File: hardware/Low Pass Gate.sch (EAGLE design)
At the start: 99 parts, among them IC1 TL072, IC2 LM397, IC3 TL072, IC4 TL072, IC5 LM397, IC6 TL072, P1 POWER_SIMPLE10_SHROUDED, Q1 112, Q2 112

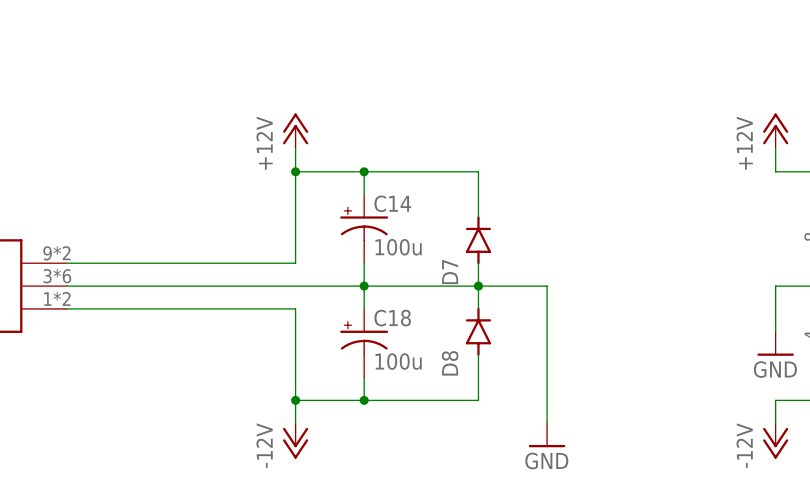
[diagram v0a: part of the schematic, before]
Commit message: use throughhole bulk caps
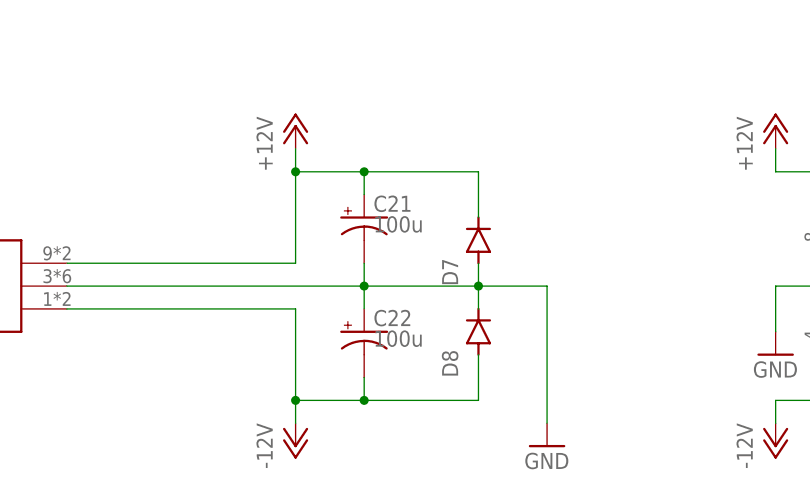
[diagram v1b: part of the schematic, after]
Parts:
- removed C14, C18: 100u, SparkFun-Passives:CAP_POLD
- added C21, C22: 100u, SparkFun-Passives:CAP_POLPTH1
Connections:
- net +12V: now also C21.+; no longer C14.+
- net -12V: now also C22.-; no longer C18.-
- net GND: now also C21.-, C22.+; no longer C14.-, C18.+

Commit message: revert to using ldr muting circuit
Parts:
- removed C21, C22: 100u, SparkFun-Passives:CAP_POLPTH1
- removed Q1, Q2: 112, barsstronics:JFET-NMMBF5484
- removed R35, R36: 0R, SparkFun-Passives:RESISTOR0603-RES
- added C14, C18: 100u, SparkFun-Passives:CAP_POLD
- added IN2NORMAL: JUMPER-PAD-2-NC_BY_TRACENO_SILK, SparkFun-Passives:JUMPER-PAD-2-NC_BY_TRACENO_SILK
- added JP1: (no value), SparkFun-Connectors:M031X03_NO_SILK
- added LDR5: VTL5CVACTROL-SMALL, optocoupler:VTL5CVACTROL-SMALL
- added LDR6: VTL5C9, optocoupler:VTL5C9
- added RA1: OPEN, SparkFun-Passives:RESISTOR0603-RES
- added TP1, TP2: TEST-POINT3X4, SparkFun-Passives:TEST-POINT3X4
- C13, C4: value 1n -> 100p
- IC1, IC3, IC4, IC6: device linear:TL072D -> linear:TL072SOIC
- LDR1, LDR2, LDR4: value VTL5C9SMALL -> VTL5CVACTROL-SMALL; device optocoupler:VTL5C9SMALL -> optocoupler:VTL5CVACTROL-SMALL
- LDR3: value VTL5C9SMALL -> VTL5C9; device optocoupler:VTL5C9SMALL -> optocoupler:VTL5C9
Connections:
- removed net N$38: Q1.D, R35.2
- removed net N$52: Q2.D, R36.2
- new net N$36: RA1.2, TP2.1
- new net N$4: RA1.1, TP1.1
- new net N$55: IN2.NORM, IN2NORMAL.1, JP1.2
- net +12V: now also C14.+; no longer C21.+
- net -12V: now also C18.-; no longer C22.-
- net GND: now also C14.-, C18.+, JP1.1, LDR3.C, LDR3.L1, LDR6.C, LDR6.L1; no longer C21.-, C22.+, Q1.S, Q2.S
- net IN-1: now also IN2NORMAL.2, JP1.3; no longer IN2.NORM
- net N$2: now also LDR4.C; no longer LDR3.C
- net N$25: now also LDR4.L2; no longer LDR3.L2
- net N$27: now also LDR5.L1; no longer LDR4.L1
- net N$3: now also LDR4.A, LDR5.C; no longer LDR3.A, LDR4.C
- net N$30: now also LDR6.A; no longer Q2.G
- net N$31: now also LDR4.L1, LDR5.L2, LDR6.L2; no longer LDR3.L1, LDR4.L2, R36.1
- net N$44: now also LDR3.L2; no longer R35.1
- net N$46: now also LDR3.A; no longer Q1.G
- net N$7: now also LDR5.A; no longer LDR4.A
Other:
- moved on the sheet: LDR3, LDR4

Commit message: update to rev E
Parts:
- removed C17, C20, C7, C9: 100n, SparkFun-Passives:CAP0805
- removed IC1, IC3, IC4, IC6: TL072, linear:TL072SOIC
- removed IN2NORMAL: JUMPER-PAD-2-NC_BY_TRACENO_SILK, SparkFun-Passives:JUMPER-PAD-2-NC_BY_TRACENO_SILK
- removed JP1: (no value), SparkFun-Connectors:M031X03_NO_SILK
- removed LEDI1, LEDI2: 5K, SparkFun-Electromechanical:POTTRIM
- removed R23, R6: 500R (opt), SparkFun-Passives:RESISTOR0603-RES
- removed RA1: OPEN, SparkFun-Passives:RESISTOR0603-RES
- removed TP1, TP2, TRIGGERREF1, TRIGGERREF2: TEST-POINT3X4, SparkFun-Passives:TEST-POINT3X4
- added C21, C22: 560p, SparkFun-Passives:CAP0805
- added U1, U2: OPAMP-QUADSO14, barsstronics:OPAMP-QUADSO14
- CTRL1, CTRL2, IN1, IN2: value AUDIO-JACKINLINE -> AUDIO-JACKINLINE-FLOATGND; device erthenvar:AUDIO-JACKINLINE -> erthenvar:AUDIO-JACKINLINE-FLOATGND
- LDR1, LDR2, LDR4, LDR5: value VTL5CVACTROL-SMALL -> VTL5C9SMALL; device optocoupler:VTL5CVACTROL-SMALL -> optocoupler:VTL5C9SMALL
- LDR3, LDR6: value VTL5C9 -> VTL5C9SMALL; device optocoupler:VTL5C9 -> optocoupler:VTL5C9SMALL
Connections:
- removed net N$19: LEDI2.E, R23.1
- removed net N$36: RA1.2, TP2.1
- removed net N$37: LEDI1.E, R6.1
- removed net N$4: RA1.1, TP1.1
- removed net N$55: IN2.NORM, IN2NORMAL.1, JP1.2
- net +12V: now also U1PWR.VCC, U2PWR.VCC; no longer C17.1, C7.1, IC1P.V+, IC3P.V+, IC4P.V+, IC6P.V+
- net -12V: now also U1PWR.VEE, U2PWR.VEE; no longer C20.2, C9.2, IC1P.V-, IC3P.V-, IC4P.V-, IC6P.V-
- net GND: now also U1D.+IN, U2D.+IN; no longer C17.2, C20.1, C7.2, C9.1, IC1A.+IN, IC4A.+IN, JP1.1, LEDI1.A, LEDI1.S, LEDI2.A, LEDI2.S
- net IN-1: now also IN2.NORM; no longer IN2NORMAL.2, JP1.3
- net N$1: now also U2D.-IN; no longer IC4A.-IN
- net N$17: no longer TRIGGERREF2.1
- net N$18: now also U1D.-IN; no longer IC1A.-IN
- net N$2: now also U2C.OUT; no longer IC4B.OUT
- net N$24: now also U2A.+IN; no longer IC6A.+IN
- net N$25: now also U2B.+IN; no longer IC6B.+IN
- net N$27: now also U2A.-IN, U2A.OUT; no longer IC6A.-IN, IC6A.OUT
- net N$28: now also C22.1, U2B.-IN, U2B.OUT; no longer IC6B.-IN, IC6B.OUT
- net N$31: now also C22.2
- net N$32: no longer TRIGGERREF1.1
- net N$40: now also U1A.+IN; no longer IC3A.+IN
- net N$41: now also U1B.+IN; no longer IC3B.+IN
- net N$42: now also U1A.-IN, U1A.OUT; no longer IC3A.-IN, IC3A.OUT
- net N$43: now also C21.1, U1B.-IN, U1B.OUT; no longer IC3B.-IN, IC3B.OUT
- net N$44: now also C21.2
- net N$48: now also U1C.OUT; no longer IC1B.OUT
- net N$53: now also U1C.-IN; no longer IC1B.-IN, R6.2
- net N$6: now also U2C.-IN; no longer IC4B.-IN, R23.2
- net VSIG: now also U2C.+IN, U2D.OUT; no longer IC4A.OUT, IC4B.+IN
- net VSIG1: now also U1C.+IN, U1D.OUT; no longer IC1A.OUT, IC1B.+IN
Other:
- moved on the sheet: R27, R9

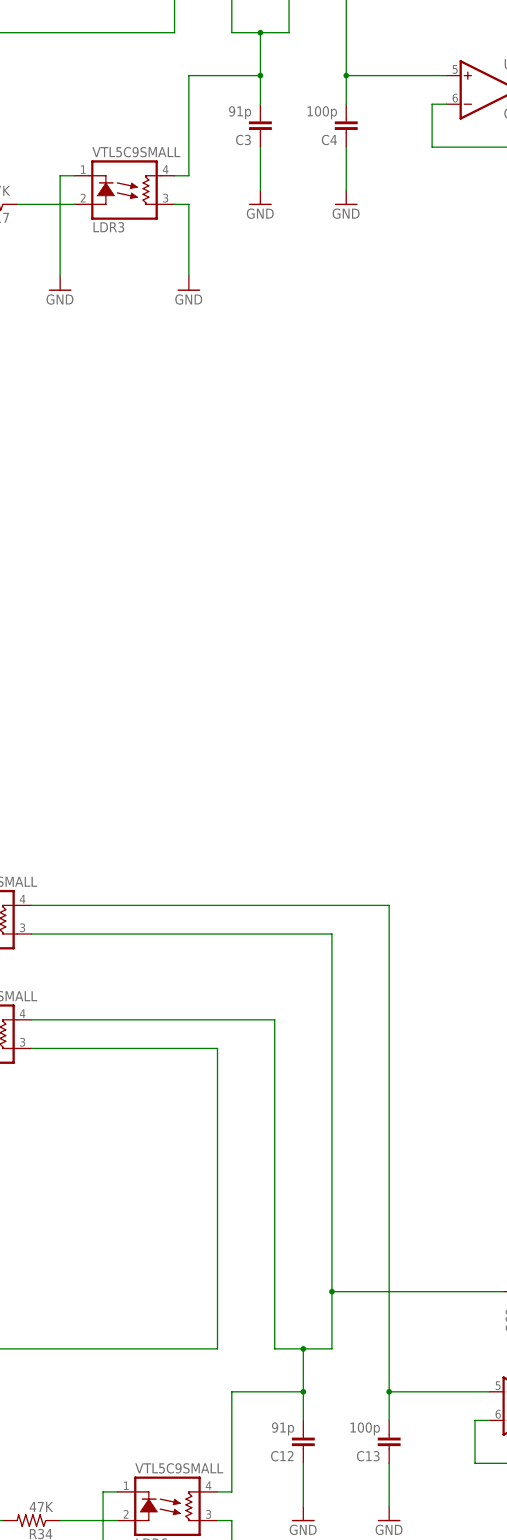
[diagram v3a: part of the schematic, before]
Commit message: updated BOM for rev E
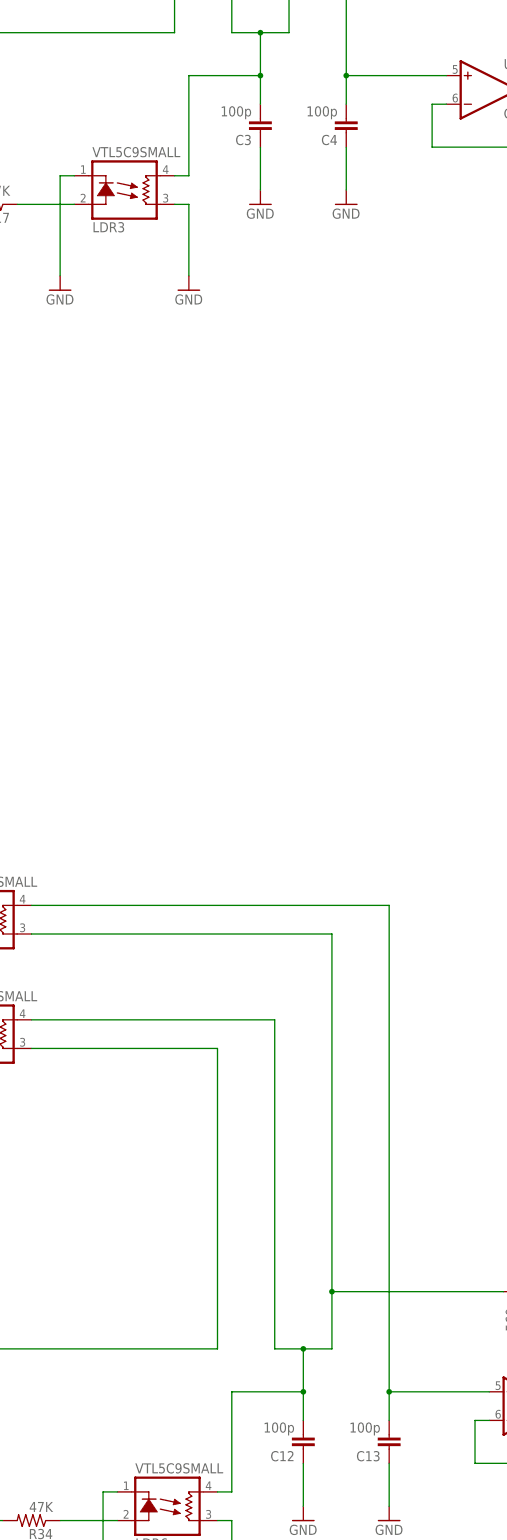
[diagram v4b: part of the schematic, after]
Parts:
- C12, C3: value 91p -> 100p
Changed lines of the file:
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@@
 <part name="GND39" library="supply1" library_urn="urn:adsk.eagle:library:371" deviceset="GND" device=""/>
 <part name="C11" library="SparkFun-Passives" deviceset="CAP" device="0805" value="1u"/>
-<part name="C12" library="SparkFun-Passives" deviceset="CAP" device="0805" value="91p"/>
+<part name="C12" library="SparkFun-Passives" deviceset="CAP" device="0805" value="100p"/>
 <part name="GND41" library="supply1" library_urn="urn:adsk.eagle:library:371" deviceset="GND" device=""/>
 <part name="GND48" library="supply1" library_urn="urn:adsk.eagle:library:371" deviceset="GND" device=""/>
@@
 <part name="GND15" library="supply1" library_urn="urn:adsk.eagle:library:371" deviceset="GND" device=""/>
 <part name="C2" library="SparkFun-Passives" deviceset="CAP" device="0805" value="1u"/>
-<part name="C3" library="SparkFun-Passives" deviceset="CAP" device="0805" value="91p"/>
+<part name="C3" library="SparkFun-Passives" deviceset="CAP" device="0805" value="100p"/>
 <part name="GND17" library="supply1" library_urn="urn:adsk.eagle:library:371" deviceset="GND" device=""/>
 <part name="GND23" library="supply1" library_urn="urn:adsk.eagle:library:371" deviceset="GND" device=""/>

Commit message: media diagrams, pdfs, clean up schm
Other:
- note added: "Low Pass Gate Revision E Author: Jacob Barss-Bailey"
- moved on the sheet: C10, C11, C12, C13, C14, C15, C16, C18, C19, C22, C5, C6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

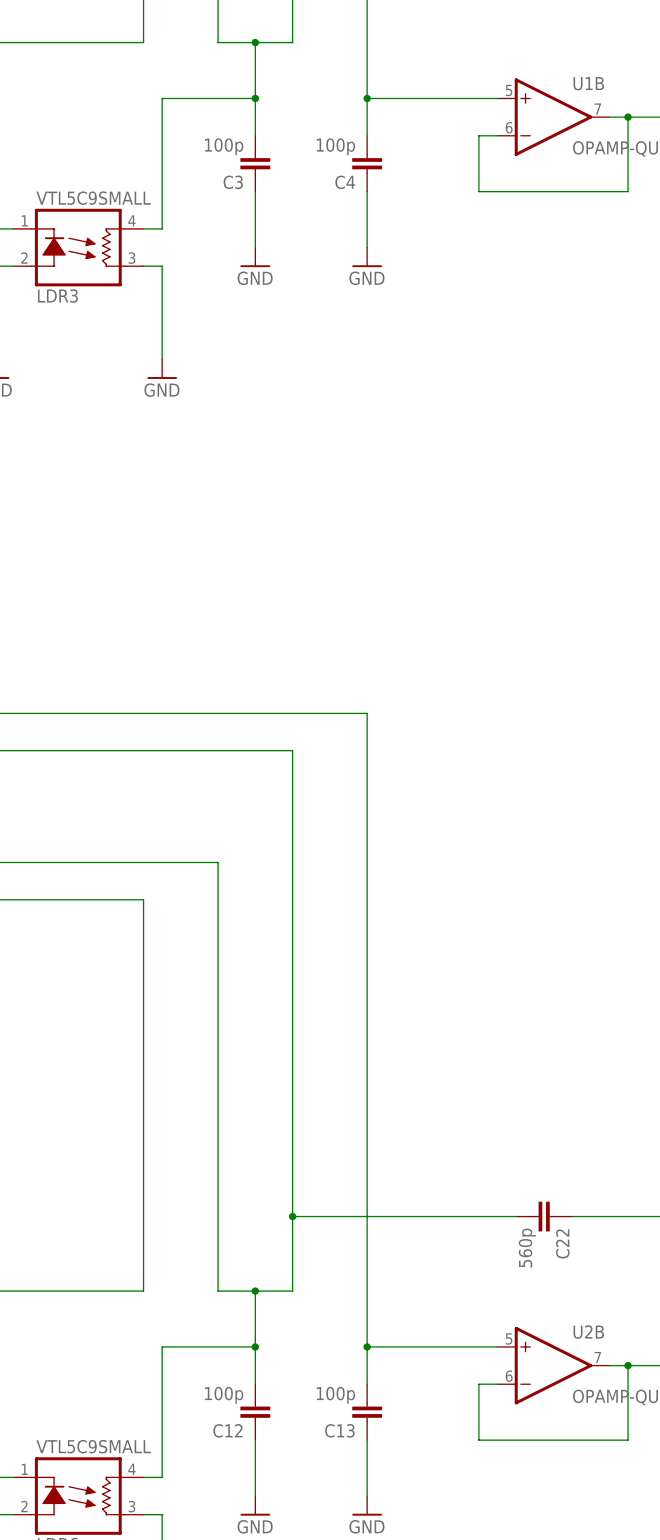
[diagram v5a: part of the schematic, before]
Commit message: fix C4/C13 value (that was resulting in 5.6x f(c) in filter)
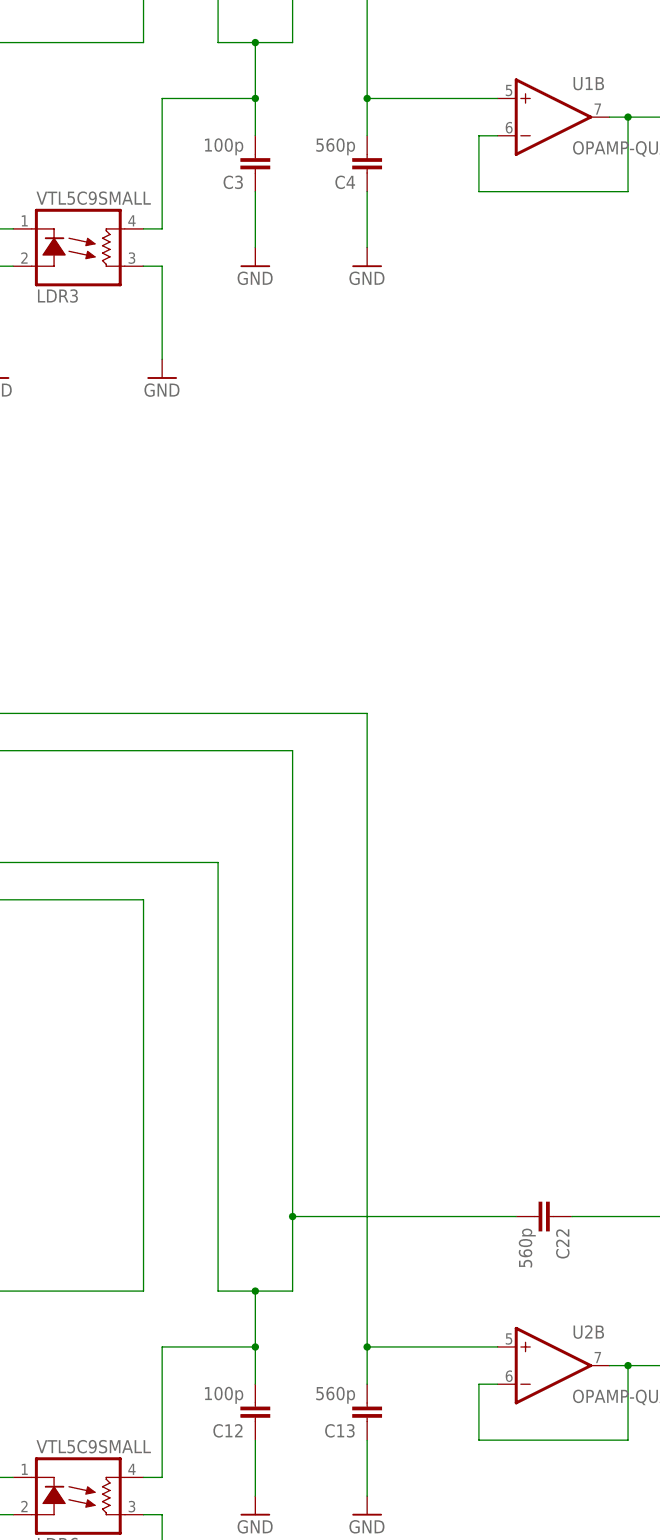
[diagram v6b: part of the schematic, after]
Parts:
- C13, C4: value 100p -> 560p
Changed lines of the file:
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@@
 <part name="LDR5" library="optocoupler" deviceset="VTL5C*" device="SMALL" technology="9" value="VTL5C9SMALL"/>
 <part name="LDR4" library="optocoupler" deviceset="VTL5C*" device="SMALL" technology="9" value="VTL5C9SMALL"/>
-<part name="C13" library="SparkFun-Passives" deviceset="CAP" device="0805" value="100p"/>
+<part name="C13" library="SparkFun-Passives" deviceset="CAP" device="0805" value="560p"/>
 <part name="GND42" library="supply1" library_urn="urn:adsk.eagle:library:371" deviceset="GND" device=""/>
 <part name="R31" library="SparkFun-Passives" deviceset="RESISTOR" device="0603-RES" value="10K"/>
@@
 <part name="LDR2" library="optocoupler" deviceset="VTL5C*" device="SMALL" technology="9" value="VTL5C9SMALL"/>
 <part name="LDR1" library="optocoupler" deviceset="VTL5C*" device="SMALL" technology="9" value="VTL5C9SMALL"/>
-<part name="C4" library="SparkFun-Passives" deviceset="CAP" device="0805" value="100p"/>
+<part name="C4" library="SparkFun-Passives" deviceset="CAP" device="0805" value="560p"/>
 <part name="GND18" library="supply1" library_urn="urn:adsk.eagle:library:371" deviceset="GND" device=""/>
 <part name="R14" library="SparkFun-Passives" deviceset="RESISTOR" device="0603-RES" value="10K"/>

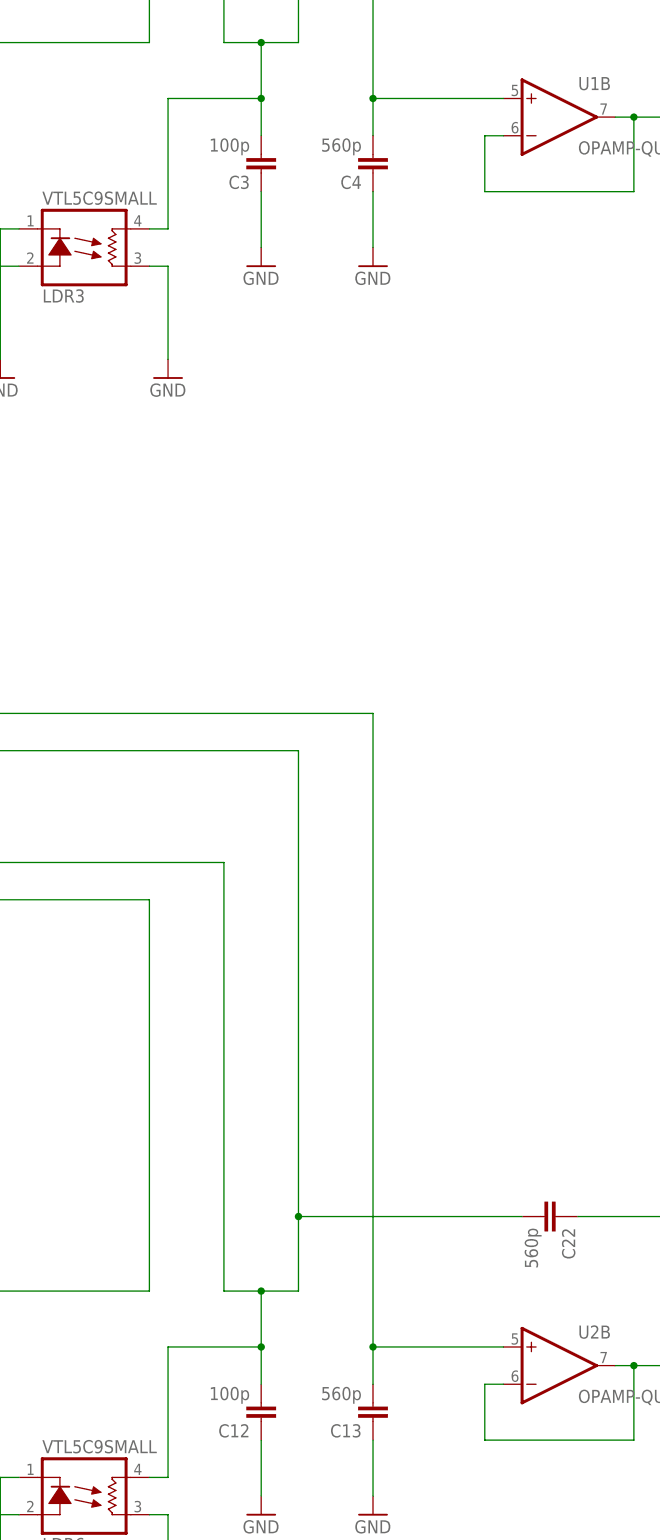
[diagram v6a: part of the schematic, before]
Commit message: Additional fix for C4/C13 value causing audio bleedthrough at low mute settings
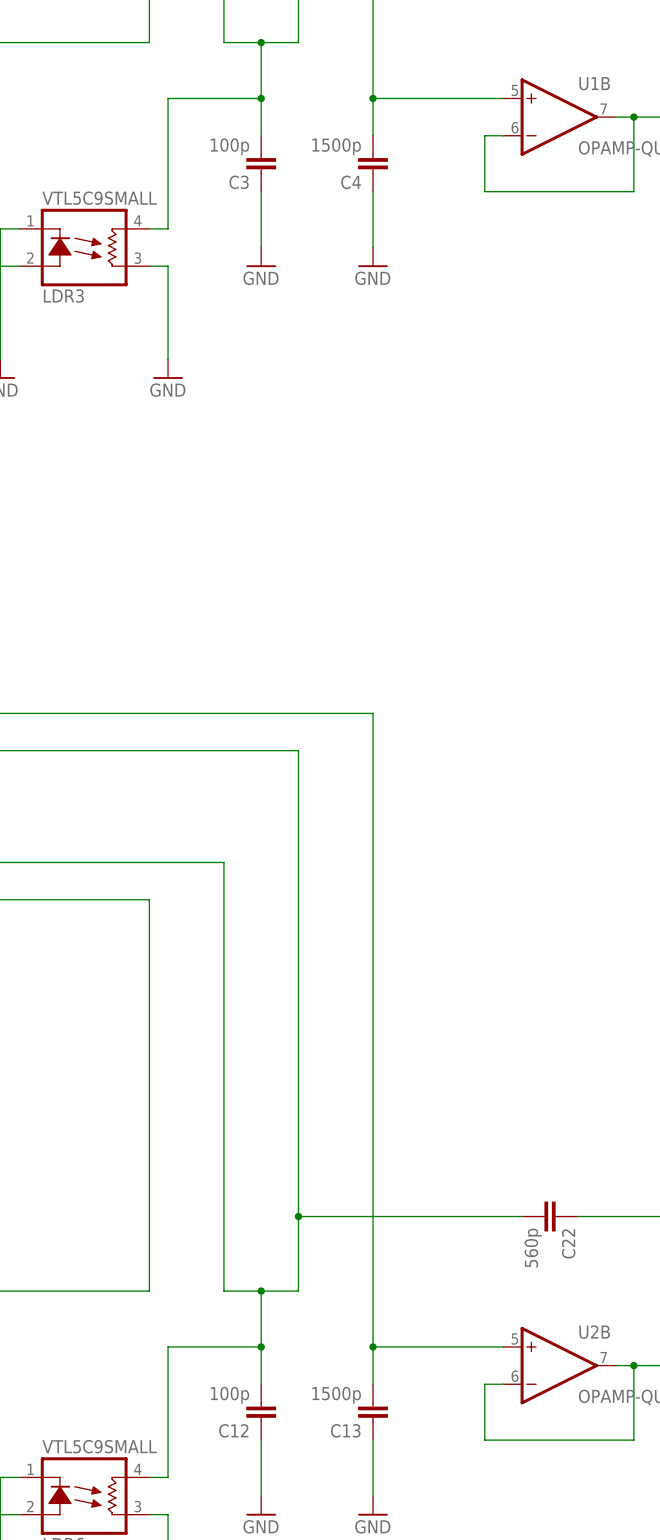
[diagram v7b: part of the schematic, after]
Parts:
- C13, C4: value 560p -> 1500p
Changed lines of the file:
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@@
 <part name="LDR5" library="optocoupler" deviceset="VTL5C*" device="SMALL" technology="9" value="VTL5C9SMALL"/>
 <part name="LDR4" library="optocoupler" deviceset="VTL5C*" device="SMALL" technology="9" value="VTL5C9SMALL"/>
-<part name="C13" library="SparkFun-Passives" deviceset="CAP" device="0805" value="560p"/>
+<part name="C13" library="SparkFun-Passives" deviceset="CAP" device="0805" value="1500p"/>
 <part name="GND42" library="supply1" library_urn="urn:adsk.eagle:library:371" deviceset="GND" device=""/>
 <part name="R31" library="SparkFun-Passives" deviceset="RESISTOR" device="0603-RES" value="10K"/>
@@
 <part name="LDR2" library="optocoupler" deviceset="VTL5C*" device="SMALL" technology="9" value="VTL5C9SMALL"/>
 <part name="LDR1" library="optocoupler" deviceset="VTL5C*" device="SMALL" technology="9" value="VTL5C9SMALL"/>
-<part name="C4" library="SparkFun-Passives" deviceset="CAP" device="0805" value="560p"/>
+<part name="C4" library="SparkFun-Passives" deviceset="CAP" device="0805" value="1500p"/>
 <part name="GND18" library="supply1" library_urn="urn:adsk.eagle:library:371" deviceset="GND" device=""/>
 <part name="R14" library="SparkFun-Passives" deviceset="RESISTOR" device="0603-RES" value="10K"/>
